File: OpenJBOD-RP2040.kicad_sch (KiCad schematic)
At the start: 58 parts, among them J1 ATX-24, J2 Bus_PCI_Express_x1, J3 Conn_02x02_Counter_Clockwise, J4 UART, J8 USB_B_Micro, J9 TEMP1, Q1 MMBT3904, Q2 MMBT3904, SW1 SW_Push, SW2 TC-6615-6-260G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

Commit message: rev4.2
Updated silkscreen info block
Changed microUSB header to MicroXNJ
Added RoHS and WEEE marking
Moved BOOTSEL to rear IO
Moved SR latch
Moved J3 and J9 closer to the board edge, this helps to not interrupt
the 12v plane on inner layer 2
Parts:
- removed SW1: SW_Push, Button_Switch_SMD:SW_Push_1P1T_XKB_TS-1187A, symbol Switch:SW_Push
- added SW1: TC-6615-6-260G, OpenJBOD_Library:KEY-TH_TC-6615-6-160G, symbol OpenJBOD:TC-6615-6-260G
- C39: JLCPCB_PN C110229 -> C2836440
- D1: JLCPCB_PN (none) -> C2764899
- D2, D3: JLCPCB_PN C8678 -> C2480
- J4: JLCPCB_PN C92159 -> C2894945
- J8: footprint Connector_USB:USB_Micro-B_Amphenol_10118194_Horizontal -> OpenJBOD_Library:MICRO-USB-SMD_MICROXNJ; JLCPCB_PN C132563 -> C404969
- U2: JLCPCB_PN (none) -> C6186
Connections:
- net GND: now also J4.1 (Pin_1), SW1.1, SW1.3 (SH), SW1.4 (SH); no longer J4.3 (Pin_3)
- net UART_RX: now also J4.2 (Pin_2); no longer J4.1 (Pin_1)
- net UART_TX: now also J4.3 (Pin_3); no longer J4.2 (Pin_2)
- net at R8.2: now also SW1.2
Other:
- moved on the sheet: J9, R31, R7, U8

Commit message: added pulldowns to SR latch pins
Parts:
- added R32, R33, R34, R35: 10k, symbol Device:R_Small
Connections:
- net GND: now also R32.2, R33.2, R34.2, R35.2
- net LOUT: now also R32.1
- net LRESET: now also R35.1
- net LSET: now also R34.1
- net ~{LOUT}: now also R33.1

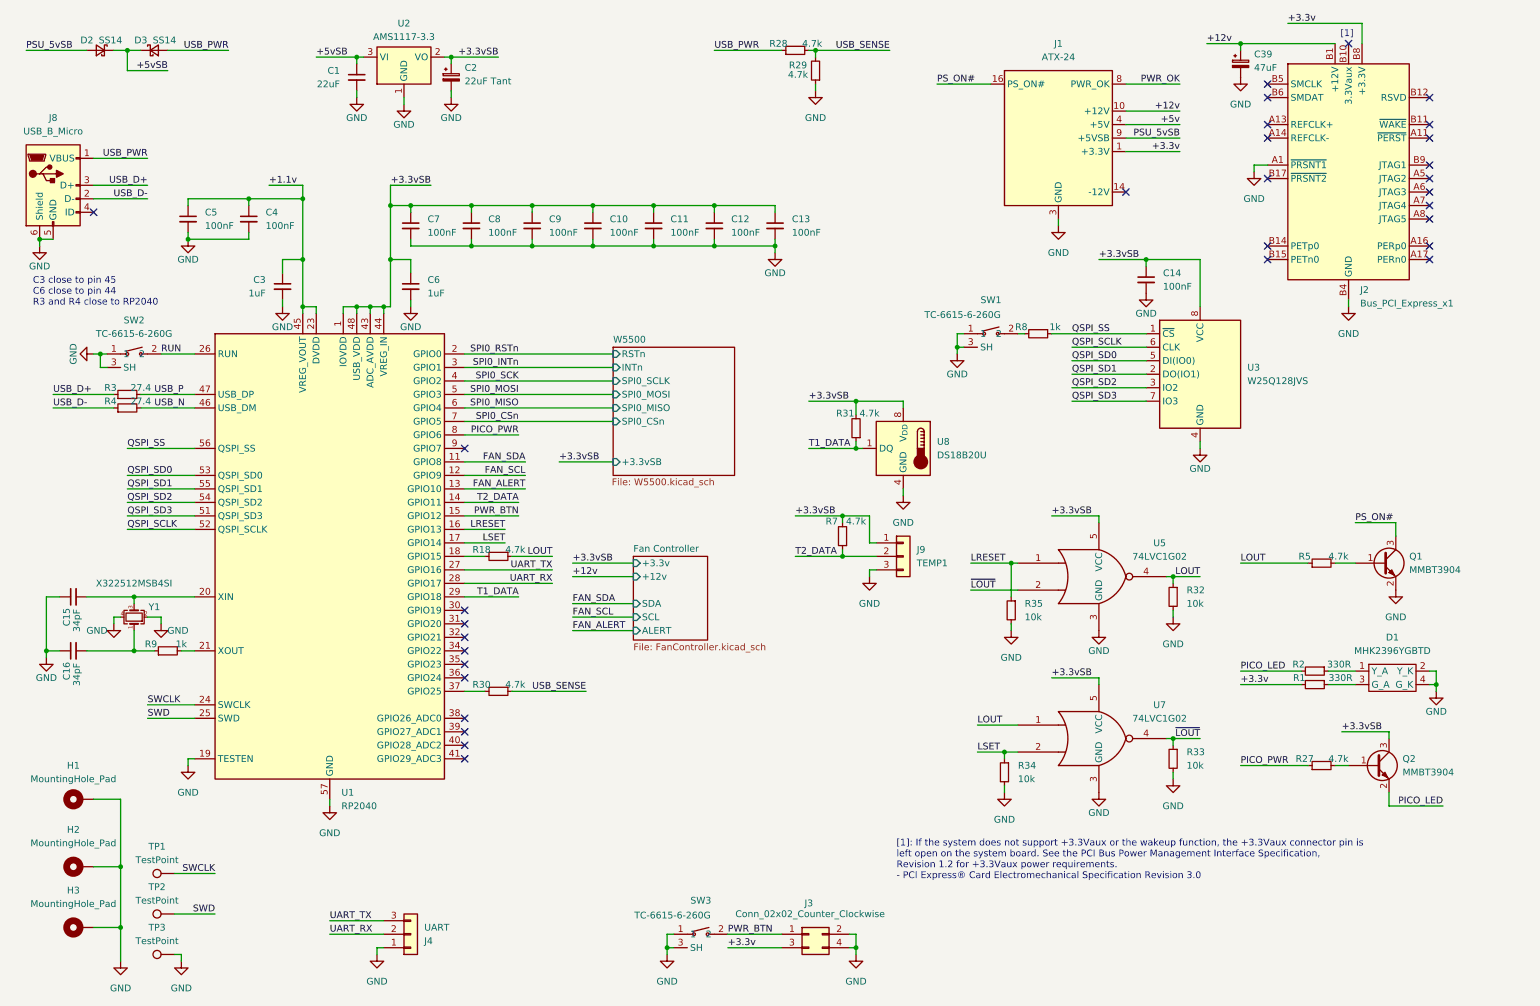
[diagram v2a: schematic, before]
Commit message: usb-c schematic changes
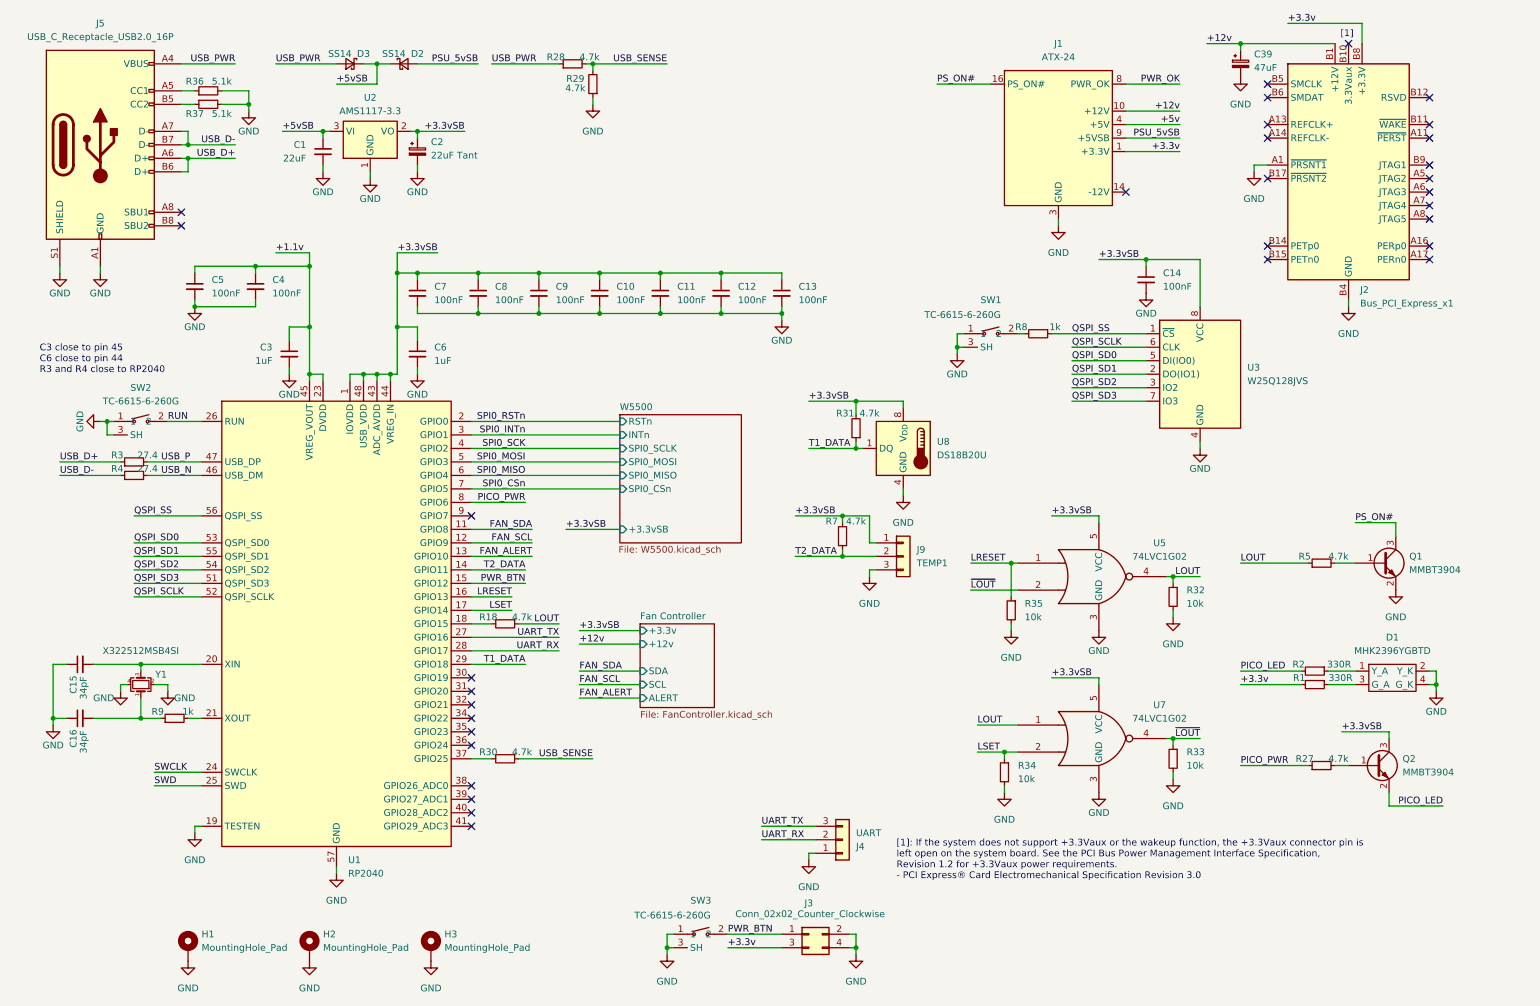
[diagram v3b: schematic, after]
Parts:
- removed J8: USB_B_Micro, OpenJBOD_Library:MICRO-USB-SMD_MICROXNJ, symbol Connector:USB_B_Micro
- removed TP1, TP2, TP3: TestPoint, TestPoint:TestPoint_Pad_D1.0mm, symbol Connector:TestPoint
- added J5: USB_C_Receptacle_USB2.0_16P, symbol Connector:USB_C_Receptacle_USB2.0_16P
- added R36, R37: 5.1k, symbol Device:R_Small
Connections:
- net GND: now also J5.A1 (GND), J5.A12 (GND), J5.B1 (GND), J5.B12 (GND), J5.S1 (SHIELD), R36.2, R37.2
- net USB_D+: now also J5.A6 (D+), J5.B6 (D+)
- net USB_D-: now also J5.A7 (D-), J5.B7 (D-)
- net USB_PWR: now also J5.A4 (VBUS), J5.A9 (VBUS), J5.B4 (VBUS), J5.B9 (VBUS)
- new net: J5.A5 (CC1), R36.1
- new net: J5.B5 (CC2), R37.1
- no-connect marks 31 -> 32
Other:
- moved on the sheet: C1, C10, C11, C12, C13, C15, C16, C2, C3, C4, C5, C6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

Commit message: pcb: usb-c, pull-downs
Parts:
- J5: footprint (none) -> OpenJBOD_Library:USB-C-SMD_TYPE-C16PIN
- R32, R33, R34, R35, R36, R37: footprint (none) -> Capacitor_SMD:C_0402_1005Metric
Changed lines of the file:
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@@
 			)
 		)
-		(property "Footprint" ""
+		(property "Footprint" "OpenJBOD_Library:USB-C-SMD_TYPE-C16PIN"
 			(at 31.75 36.83 0)
 			(effects
@@
 		)
 		(instances
-			(project ""
+			(project "OpenJBOD-RP2040"
 				(path "/341cb12b-c598-4bc6-a9bc-01f338de5a85"
 					(reference "J5")
@@
 			)
 		)
-		(property "Footprint" ""
+		(property "Footprint" "Capacitor_SMD:C_0402_1005Metric"
 			(at 229.87 152.4 0)
 			(effects
@@
 			)
 		)
-		(property "Footprint" ""
+		(property "Footprint" "Capacitor_SMD:C_0402_1005Metric"
 			(at 48.26 29.21 0)
 			(effects
@@
 			)
 		)
-		(property "Footprint" ""
+		(property "Footprint" "Capacitor_SMD:C_0402_1005Metric"
 			(at 229.87 121.92 0)
 			(effects
@@
 		)
 		(instances
-			(project ""
+			(project "OpenJBOD-RP2040"
 				(path "/341cb12b-c598-4bc6-a9bc-01f338de5a85"
 					(reference "R32")
@@
 			)
 		)
-		(property "Footprint" ""
+		(property "Footprint" "Capacitor_SMD:C_0402_1005Metric"
 			(at 48.26 26.67 0)
 			(effects
@@
 		)
 		(instances
-			(project ""
+			(project "OpenJBOD-RP2040"
 				(path "/341cb12b-c598-4bc6-a9bc-01f338de5a85"
 					(reference "R36")
@@
 			)
 		)
-		(property "Footprint" ""
+		(property "Footprint" "Capacitor_SMD:C_0402_1005Metric"
 			(at 199.39 124.46 0)
 			(effects
@@
 		)
 		(instances
-			(project ""
+			(project "OpenJBOD-RP2040"
 				(path "/341cb12b-c598-4bc6-a9bc-01f338de5a85"
 					(reference "#PWR064")
@@
 			)
 		)
-		(property "Footprint" ""
+		(property "Footprint" "Capacitor_SMD:C_0402_1005Metric"
 			(at 198.12 154.94 0)
 			(effects
